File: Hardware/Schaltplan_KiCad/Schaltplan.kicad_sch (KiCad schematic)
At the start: 15 parts, among them J1 3-106505-2, J2 3-106505-2, J3 Conn_01x02_Pin, J4 Conn_01x02_Pin, U1 MCP2562-E-SN, U2 MCP2562-E-SN, U3 ESP32-DEVKITC-32U

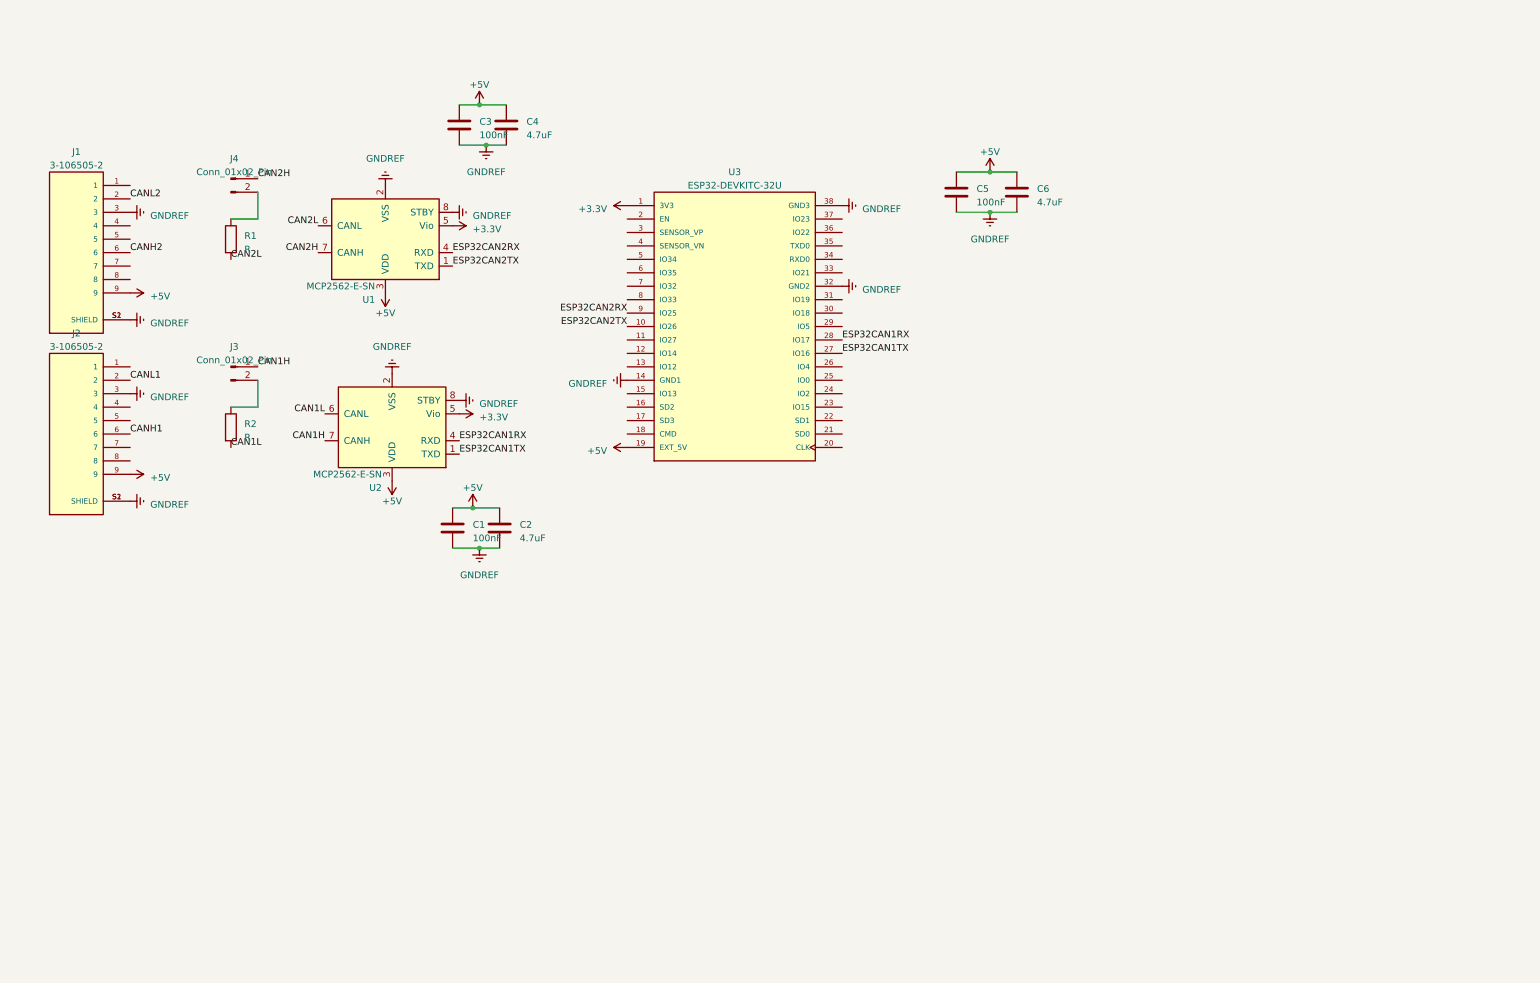
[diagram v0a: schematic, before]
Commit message: added power supply and uart communication
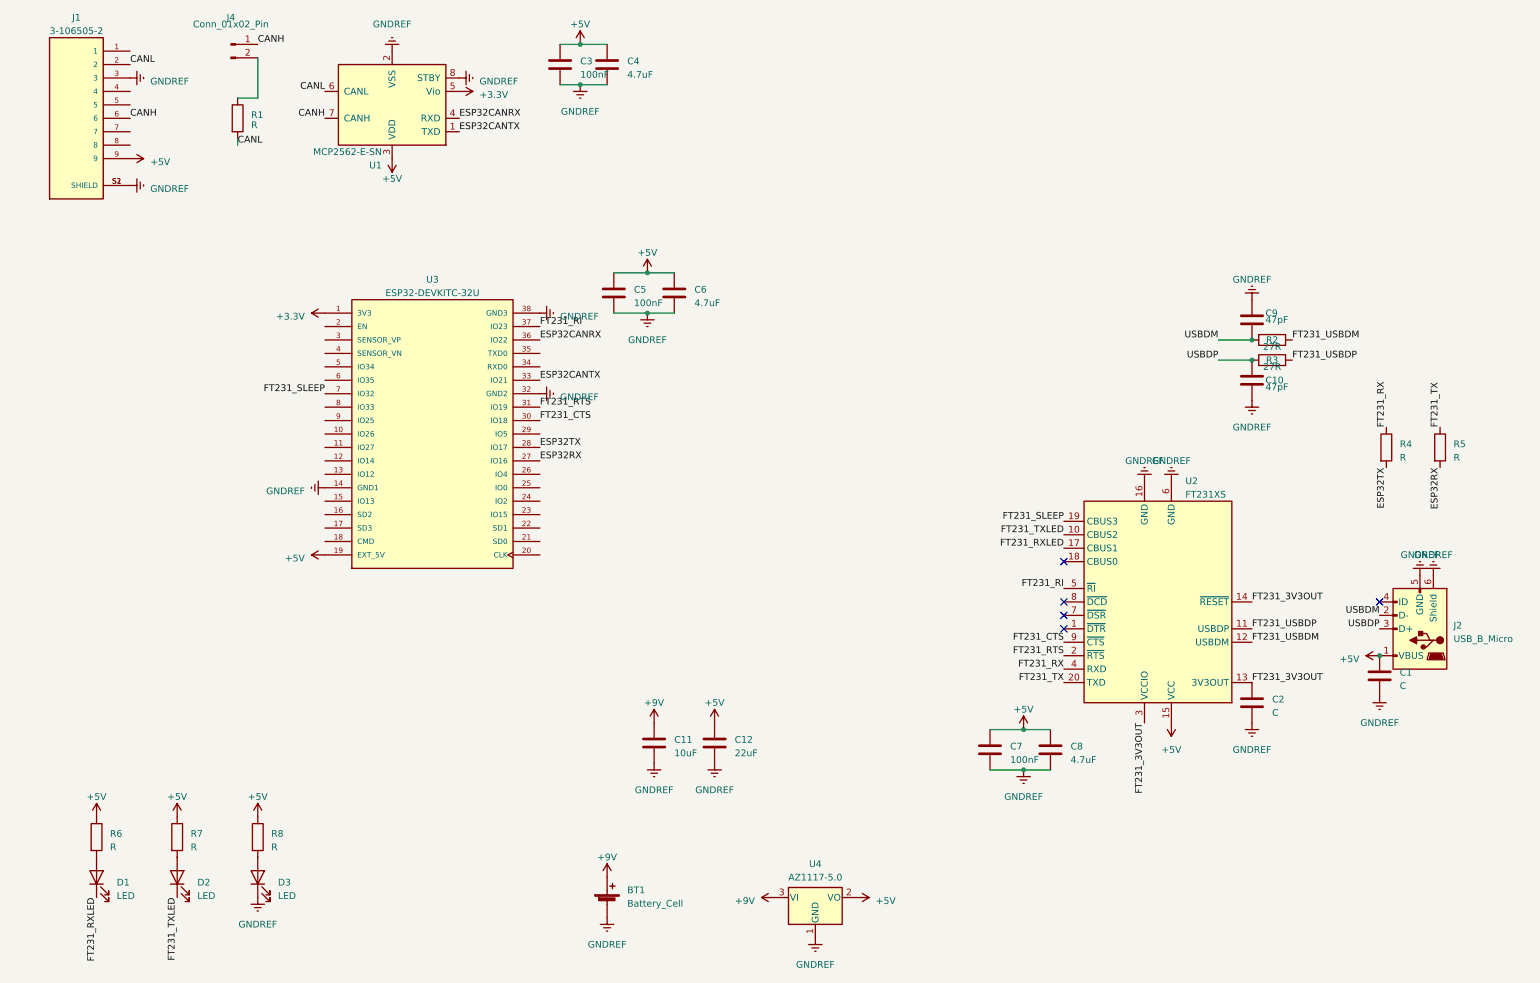
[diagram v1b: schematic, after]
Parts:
- removed J2: 3-106505-2, TE_3-106505-2, symbol 3-106505-2:3-106505-2
- removed J3: Conn_01x02_Pin, symbol Connector:Conn_01x02_Pin
- removed U2: MCP2562-E-SN, Package_SO:SOIC-8_3.9x4.9mm_P1.27mm, symbol Interface_CAN_LIN:MCP2562-E-SN
- added BT1: Battery_Cell, symbol Device:Battery_Cell
- added C10, C9: 47pF, symbol Device:C
- added C11: 10uF, symbol Device:C
- added C12: 22uF, symbol Device:C
- added C7: 100nF, symbol Device:C
- added C8: 4.7uF, symbol Device:C
- added D1, D2, D3: LED, symbol Device:LED
- added J2: USB_B_Micro, symbol Connector:USB_B_Micro
- added R3: 27R, symbol Device:R
- added R4, R5, R6, R7, R8: R, symbol Device:R
- added U2: FT231XS, Package_SO:SSOP-20_3.9x8.7mm_P0.635mm, symbol Interface_USB:FT231XS
- added U4: AZ1117-5.0, symbol Regulator_Linear:AZ1117-5.0
- C1: value 100nF -> C
- C2: value 4.7uF -> C
- R2: value R -> 27R
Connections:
- net CANH2 is gone; now on net CANH: J1.6
- net CANL2 is gone; now on net CANL: J1.2
- net +5V: now also C12.1, C7.1, C8.1, J2.1 (VBUS), R6.1, R7.1, R8.1, U2.15 (VCC), U4.2 (VO); no longer C2.1
- net GNDREF: now also BT1.2 (-), C10.2, C11.2, C12.2, C7.2, C8.2, C9.1, D3.1 (K), J2.5 (GND), J2.6 (Shield), U2.16 (GND), U2.6 (GND), U4.1 (GND)
- net FT231_USBDM: now reaches R2.1
- net FT231_USBDM: now also U2.12 (USBDM)
- net FT231_CTS: now reaches U3.30 (IO18)
- net FT231_CTS: now also U2.9 (~{CTS})
- net FT231_RTS: now reaches U3.31 (IO19)
- net FT231_RTS: now also U2.2 (~{RTS})
- net ESP32CANTX: now reaches U3.33 (IO21)
- net ESP32CANTX: now also U1.1 (TXD)
- net ESP32CANRX: now reaches U3.36 (IO22)
- net ESP32CANRX: now also U1.4 (RXD)
- net FT231_RI: now reaches U3.37 (IO23)
- net FT231_RI: now also U2.5 (~{RI})
- net FT231_SLEEP: now reaches U3.7 (IO32)
- net FT231_SLEEP: now also U2.19 (CBUS3)
- net CAN1L renamed USBDM
- net USBDM: now also C9.2, J2.2 (D-)
- net CAN2H renamed CANH
- net CAN2L renamed CANL
- net ESP32CAN1RX renamed ESP32TX
- net ESP32TX: now also R4.2
- net ESP32CAN1TX renamed ESP32RX
- net ESP32RX: now also R5.2
- net ESP32CAN2RX: no longer names the net of U3.9 (IO25)
- net ESP32CAN2RX: no longer U1.4 (RXD)
- net ESP32CAN2TX: no longer names the net of U3.10 (IO26)
- net ESP32CAN2TX: no longer U1.1 (TXD)
- new net: D1.2 (A), R6.2
- new net: D3.2 (A), R8.2
- new net: D2.2 (A), R7.2
- new net +9V: BT1.1 (+), C11.1, U4.3 (VI)
- new net FT231_3V3OUT: C2.1, U2.13 (3V3OUT), U2.14 (~{RESET}), U2.3 (VCCIO)
- new net FT231_RX: R4.1, U2.4 (RXD)
- new net FT231_RXLED: D1.1 (K), U2.17 (CBUS1)
- new net FT231_TX: R5.1, U2.20 (TXD)
- new net FT231_TXLED: D2.1 (K), U2.10 (CBUS2)
- new net FT231_USBDP: R3.2, U2.11 (USBDP)
- new net USBDP: C10.1, J2.3 (D+), R3.1
- no-connect marks 0 -> 5
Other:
- moved on the sheet: C3, C4, C5, C6, J1, J4, R1, U1, U3

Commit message: added leds, switches and buttons
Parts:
- added C13: C, symbol Device:C
- added D4, D5, D6, D7: LED, symbol Device:LED
- added J3: Conn_01x04_Pin, symbol Connector:Conn_01x04_Pin
- added R10, R11, R9: 10k, symbol Device:R
- added R12, R13, R14: 1k, symbol Device:R
- added R15, R16, R17, R18: 270, symbol Device:R
- added S1: MINI-SPDT-SW, SW_MINI-SPDT-SW, symbol MINI-SPDT-SW:MINI-SPDT-SW
- added SW1, SW2, SW3: SW_Omron_B3FS, symbol Switch:SW_Omron_B3FS
- R6, R7, R8: value R -> 270
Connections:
- net +5V: no longer R6.1, R7.1, R8.1
- net +9V: now also S1.1; no longer BT1.1 (+)
- net CANL: now also U3.5 (IO34), C13.1
- net FT231_3V3OUT: no longer C2.1, U2.13 (3V3OUT), U2.14 (~{RESET})
- net GNDREF: now also C13.2, J3.1 (Pin_1), SW1.1, SW2.1, SW3.1
- net ESP32_IO26: now reaches U3.10 (IO26)
- net ESP32_IO26: now also R13.2
- net ESP32_IO27: now reaches U3.11 (IO27)
- net ESP32_IO27: now also R14.2
- net ESP32_IO14: now reaches U3.12 (IO14)
- net ESP32_IO14: now also D7.1 (K)
- net ESP32_IO13: now reaches U3.15 (IO13)
- net ESP32_IO13: now also D6.1 (K)
- net ESP32_IO4: now reaches U3.26 (IO4)
- net ESP32_IO4: now also D5.1 (K)
- net ESP32_IO33: now reaches U3.8 (IO33)
- net ESP32_IO33: now also D4.1 (K)
- net ESP32_IO25: now reaches U3.9 (IO25)
- net ESP32_IO25: now also R12.2
- new net: R11.2, R14.1, SW3.2
- new net: D4.2 (A), R15.2
- new net: D7.2 (A), R18.2
- new net: D6.2 (A), R17.2
- new net: R10.2, R13.1, SW2.2
- new net: D5.2 (A), R16.2
- new net: R12.1, R9.2, SW1.2
- new net +3V3: C2.1, R10.1, R11.1, R15.1, R16.1, R17.1, R18.1, R6.1, R7.1, R8.1, R9.1, U2.13 (3V3OUT), U2.14 (~{RESET})
- new net +9VBatterie: BT1.1 (+), S1.2

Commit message: Included Logic Level Shifter with Display
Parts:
- added C14: 100nF, symbol Device:C
- added C15: 4.7uF, symbol Device:C
- added R19: 200k, symbol Device:R
- added R20, R21, R22, R23: 10k, symbol Device:R
- added U5: PCA9306DCTR, SOP65P400X130-8N, symbol PCA9306DCTR:PCA9306DCTR
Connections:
- net FT231_3V3OUT is gone; now on net +3V3: U2.3 (VCCIO)
- net +3V3: now also R20.1, R21.1, U5.2 (VREF1)
- net +5V: now also J3.2 (Pin_2), C14.1, C15.1, R19.1, R22.1, R23.1
- net ESP32CANRX: now also U3.9 (IO25); no longer U3.36 (IO22)
- net ESP32CANTX: now also U3.10 (IO26); no longer U3.33 (IO21)
- net GNDREF: now also C14.2, C15.2, U5.1 (GND)
- net DISPLAY_SDA2: now reaches J3.3 (Pin_3)
- net DISPLAY_SDA2: now also R23.2, U5.5 (SDA2)
- net DISPLAY_SCL2: now reaches J3.4 (Pin_4)
- net DISPLAY_SCL2: now also R22.2, U5.6 (SCL2)
- net ESP32_IO5: now reaches U3.29 (IO5)
- net ESP32_IO5: now also R12.2
- net ESP32_IO35: now reaches U3.6 (IO35)
- net ESP32_IO35: now also R13.2
- net +9V renamed POWER_SUPPLY
- net +9VBatterie renamed +VDC
- removed net ESP32_IO25: R12.2, U3.9 (IO25)
- removed net ESP32_IO26: R13.2, U3.10 (IO26)
- new net ENABLE: R19.2, U5.7 (VREF2), U5.8 (EN)
- new net ESP32_SCL1: R21.2, U3.36 (IO22), U5.3 (SCL1)
- new net ESP32_SDA1: R20.2, U3.33 (IO21), U5.4 (SDA1)
- no-connect marks 5 -> 26

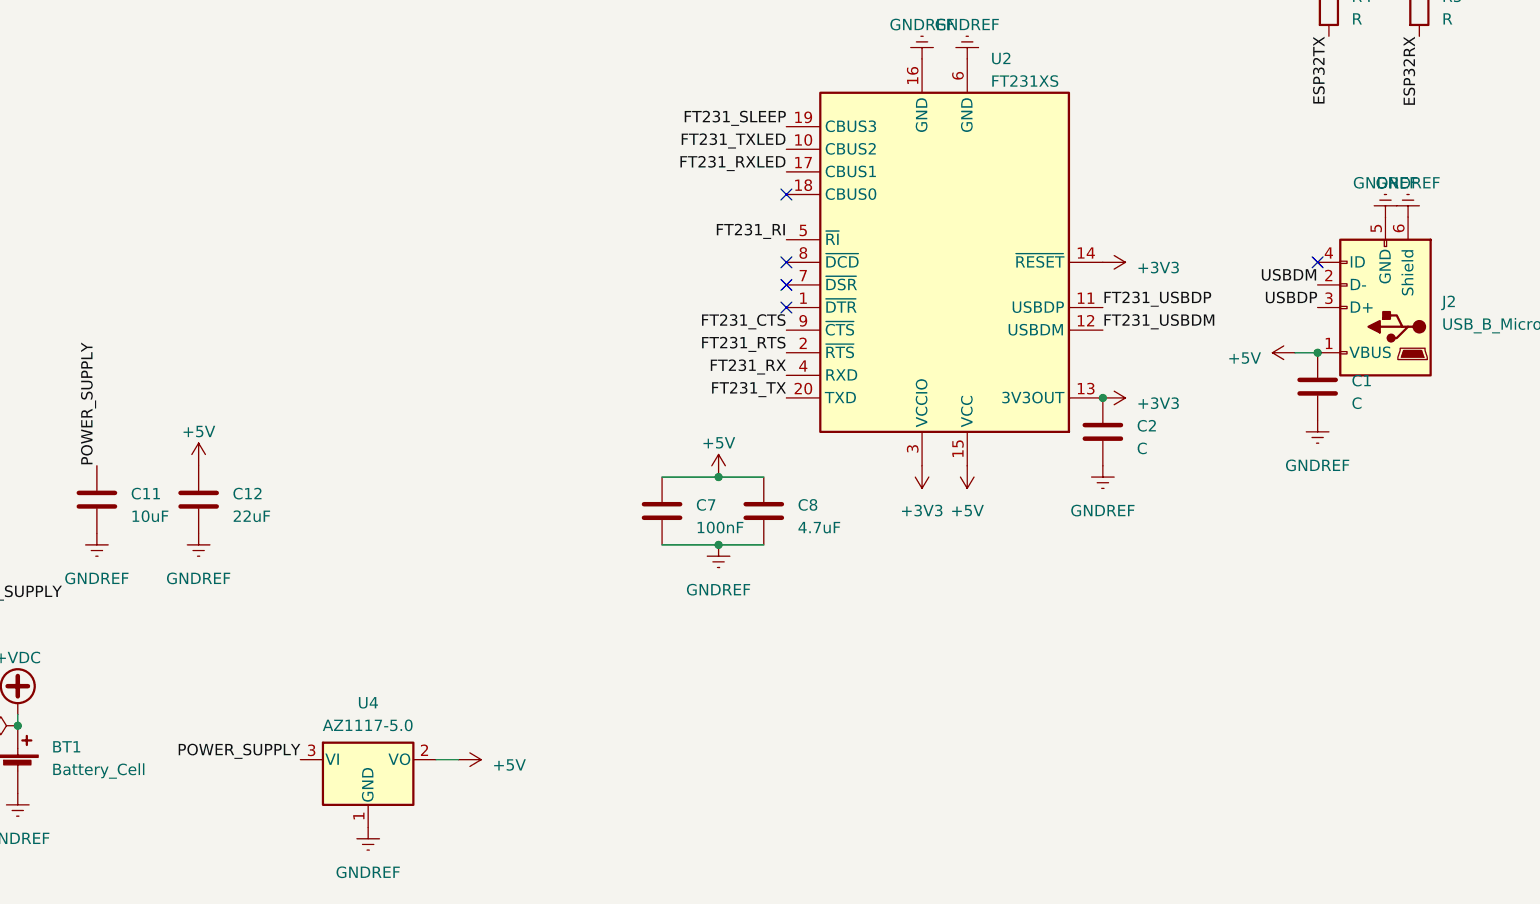
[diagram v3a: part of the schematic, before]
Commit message: added missing footprints
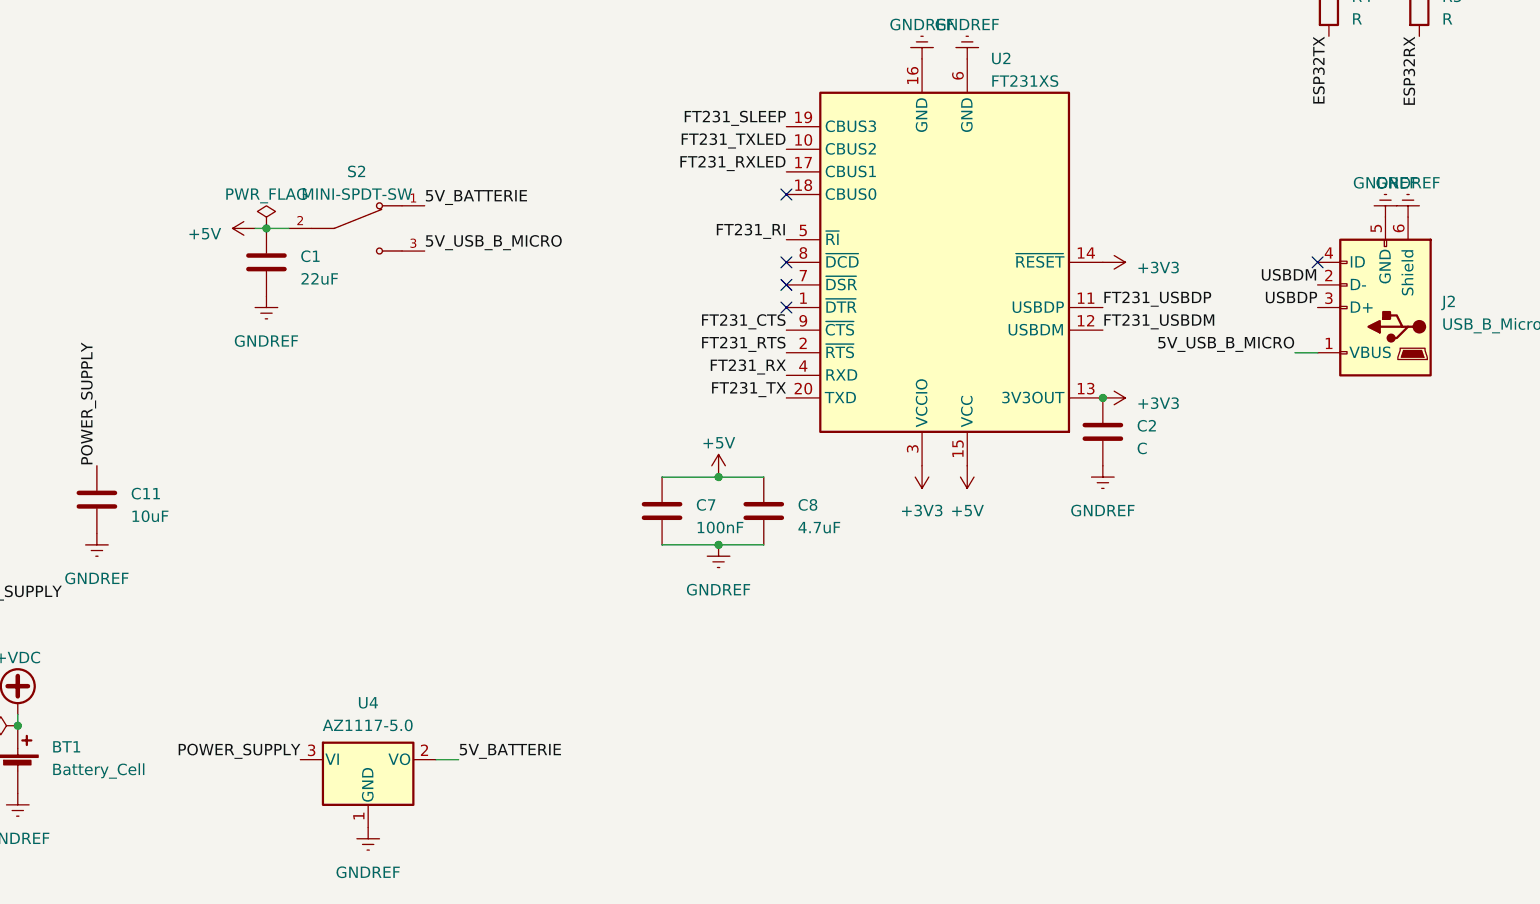
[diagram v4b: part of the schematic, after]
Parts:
- removed C12: 22uF, symbol Device:C
- added S2: MINI-SPDT-SW, switches:SW_MINI-SPDT-SW, symbol MINI-SPDT-SW:MINI-SPDT-SW
- C1: value C -> 22uF; footprint (none) -> Capacitor_SMD:C_1812_4532Metric_Pad1.57x3.40mm_HandSolder
- C10, C11, C13, C14, C15, C2, C3, C4, C5, C6, C7, C8, C9: footprint (none) -> Capacitor_SMD:C_1812_4532Metric_Pad1.57x3.40mm_HandSolder
- D1, D2, D3, D4, D5, D6, D7: footprint (none) -> LED:LED_OF-SMD3528WC
- J1: footprint TE_3-106505-2 -> Stecker:TE_3-106505-2
- J2: footprint (none) -> Connector_USB:USB_Micro-B_Amphenol_10103594-0001LF_Horizontal
- J3: footprint (none) -> Connector_PinHeader_2.54mm:PinHeader_1x04_P2.54mm_Vertical
- J4: footprint (none) -> Connector_PinHeader_2.54mm:PinHeader_1x02_P2.54mm_Vertical
- R1, R10, R11, R12, R13, R14, R15, R16, R17, R18, R19, R2, R20, R21, R22, R23, R3, R4, R5, R6, R7, R8, R9: footprint (none) -> Resistor_SMD:R_2010_5025Metric_Pad1.40x2.65mm_HandSolder
- S1: footprint SW_MINI-SPDT-SW -> switches:SW_MINI-SPDT-SW
- SW1, SW2, SW3: footprint (none) -> Button:SW_B3FS-1010P
- U1: footprint Package_SO:SOIC-8_3.9x4.9mm_P1.27mm -> Package_DIP:DIP-8_W7.62mm
- U2: footprint Package_SO:SSOP-20_3.9x8.7mm_P0.635mm -> USB2UART:SOP63P600X175-20N
- U3: footprint MODULE_ESP32-DEVKITC-32U -> ESP:MODULE_ESP32-DEVKITC-32U
- U4: footprint (none) -> LDO:SOT150P410X160-3N
- U5: footprint SOP65P400X130-8N -> Level_Shifter:SOP65P400X130-8N
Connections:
- net +5V: now also S2.2; no longer J2.1 (VBUS), U4.2 (VO)
- new net 5V_BATTERIE: S2.1, U4.2 (VO)
- new net 5V_USB_B_MICRO: J2.1 (VBUS), S2.3
